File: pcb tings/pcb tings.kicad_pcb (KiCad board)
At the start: 2 copper layers, 24 parts, among them SW1 SW_Push, U1 ATmega32U4-A, Y1 16MHz

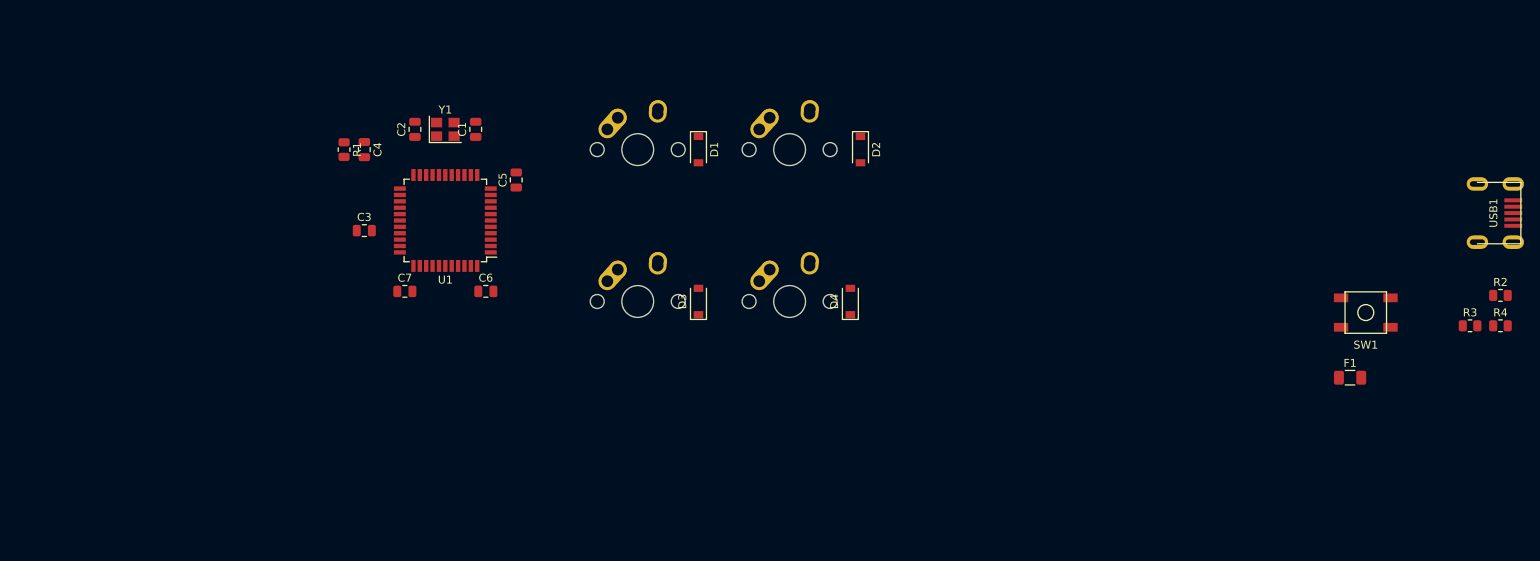
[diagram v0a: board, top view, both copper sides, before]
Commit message: creating pcb edge cuts
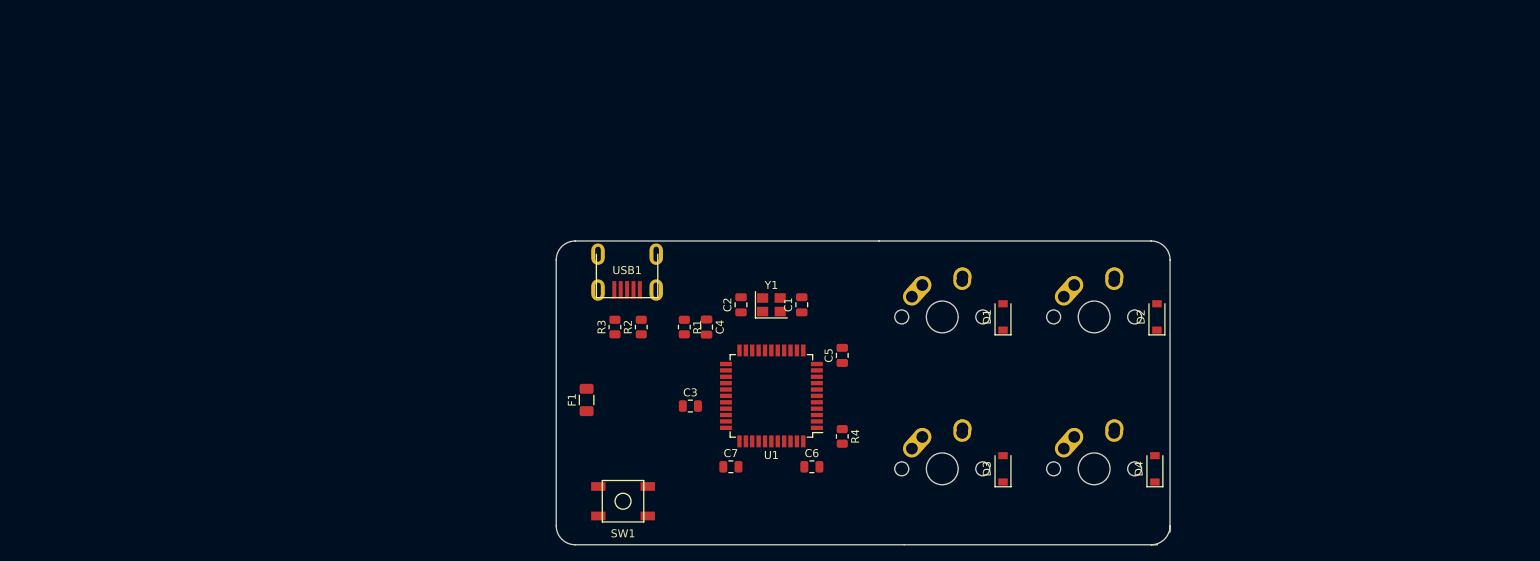
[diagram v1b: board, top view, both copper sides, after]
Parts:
- moved R2 107.8 mm to (123.4, 100.5), turned to 90 degrees
- moved R3 107.3 mm to (120.1, 100.5), turned to 90 degrees
- moved USB1 106.8 mm to (121.6, 91.3), turned to -90 degrees
- moved SW1 96.1 mm to (121.1, 122.3)
- moved F1 95.8 mm to (116.5, 109.6), turned to 90 degrees
- moved R4 83.7 mm to (148.6, 114.2), turned to -90 degrees
- moved C4 48.4 mm to (131.6, 100.5)
- moved R1 48.1 mm to (128.8, 100.5)
- moved C6 46.4 mm to (144.8, 118.0)
- moved C7 46.4 mm to (134.6, 118.0)
- moved C5 46.4 mm to (148.6, 104.0)
- moved C1 46.4 mm to (143.5, 97.7)
- moved C2 46.4 mm to (135.9, 97.7)
- moved C3 46.4 mm to (129.5, 110.4)
- moved U1 46.4 mm to (139.7, 109.1)
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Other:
- board outline added: 77 x 38.1 mm

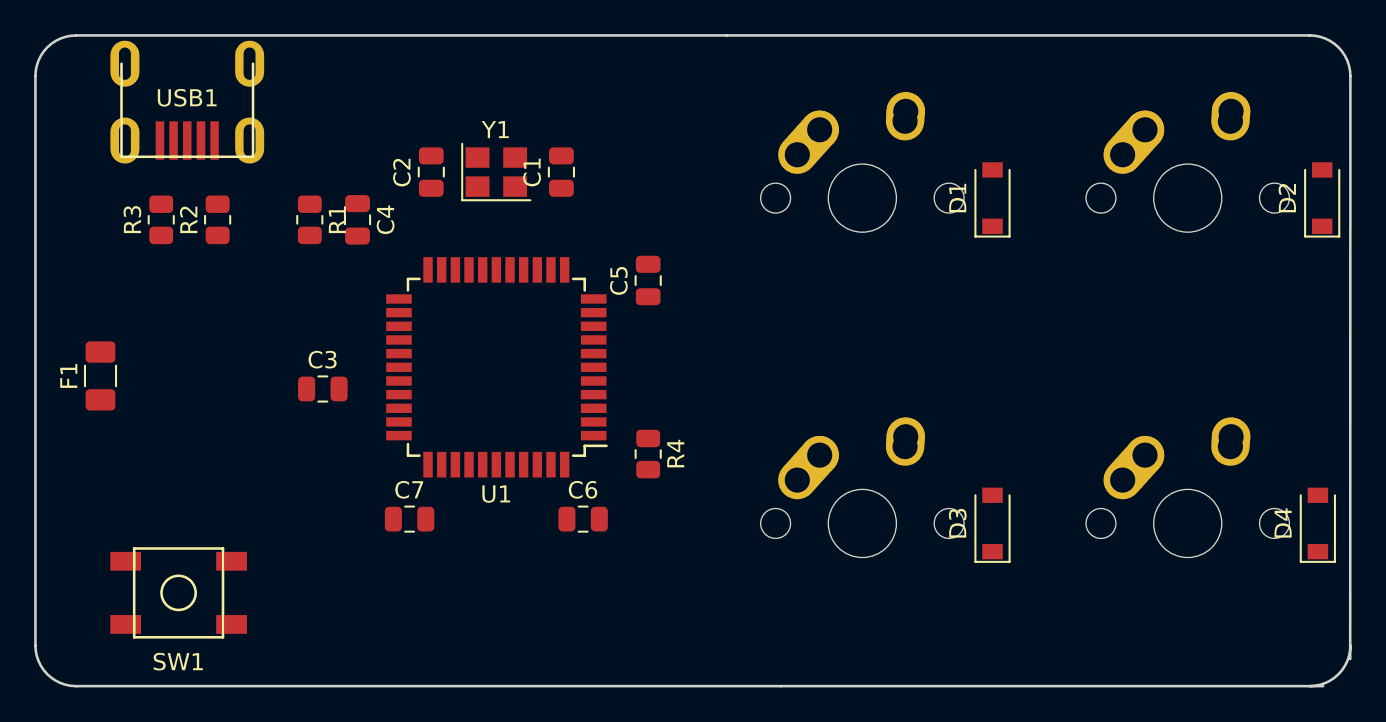
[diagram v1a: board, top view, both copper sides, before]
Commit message: Fixed footprints and edgecuts
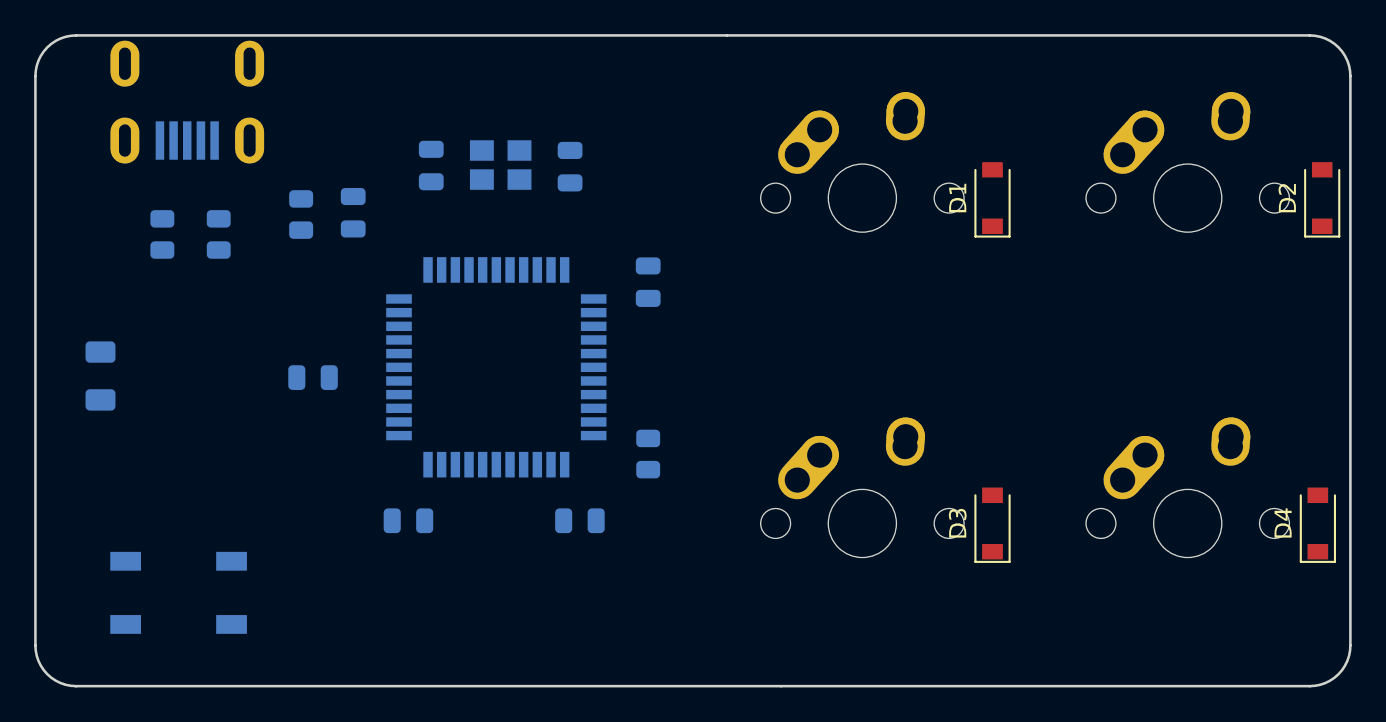
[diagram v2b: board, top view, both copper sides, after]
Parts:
- C1: renamed from C3; moved to B.Cu
- C2: renamed from C4; moved to B.Cu
- C3: renamed from C7; moved to B.Cu
- C4: renamed from C1; moved to B.Cu
- C5: renamed from C2; moved to B.Cu
- C6: renamed from C5; moved to B.Cu
- C7: renamed from C6; moved to B.Cu
- F1, R2, R4, SW1, U1, USB1, Y1: moved to B.Cu
- R1: renamed from R3; moved to B.Cu
- R3: renamed from R1; moved to B.Cu
- moved C1 19.5 mm to (144.0, 97.4), turned to 90 degrees
- moved C6 14.6 mm to (144.6, 118.1), turned to 180 degrees
- moved C5 14.2 mm to (148.6, 104.1)
- moved C4 12.4 mm to (131.3, 100.1)
- moved C7 10.2 mm to (134.6, 118.1)
- moved C3 10.0 mm to (129.0, 109.7), turned to 180 degrees
- moved R3 8.68 mm to (120.1, 101.3), turned to 90 degrees
- moved R1 8.20 mm to (128.3, 100.2)
- moved C2 5.36 mm to (135.9, 97.3)
- moved R2 0.86 mm to (123.4, 101.3)
- moved Y1 0.48 mm to (140.0, 97.3), turned to 180 degrees
- turned F1 to -90 degrees
- turned R4 to 90 degrees
- turned SW1 to 180 degrees
- turned U1 to 0 degrees
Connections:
- U1 pad 27: unconnected-(U1-Pad27) -> ROW0
- U1 pad 28: unconnected-(U1-Pad28) -> COL1
- U1 pad 29: unconnected-(U1-Pad29) -> COL0
- U1 pad 30: unconnected-(U1-Pad30) -> ROW1
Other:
- outline, holes or cut-outs redrawn

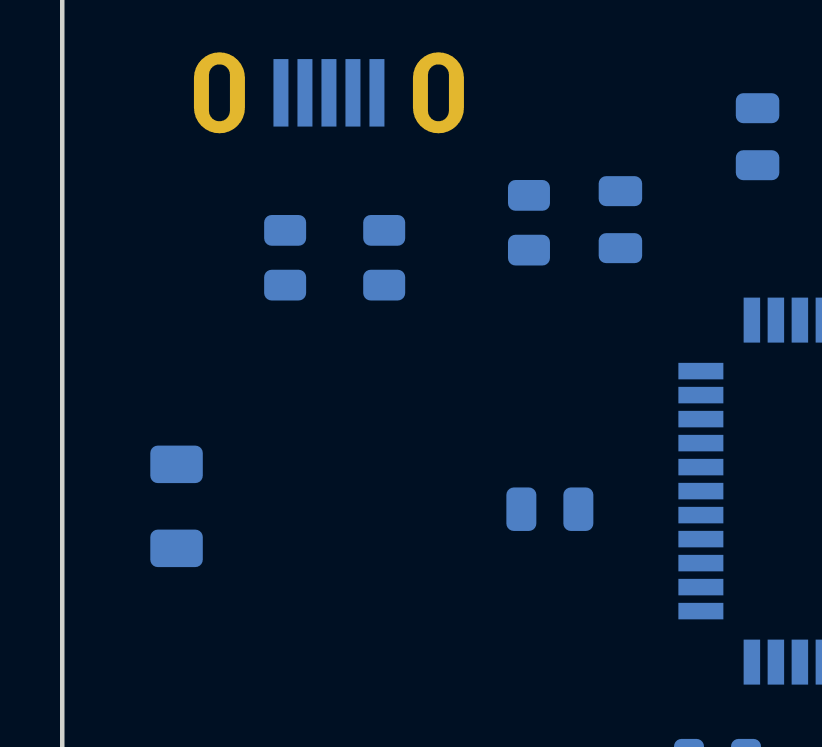
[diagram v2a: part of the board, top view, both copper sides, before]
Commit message: fixed connections (ratsnest)
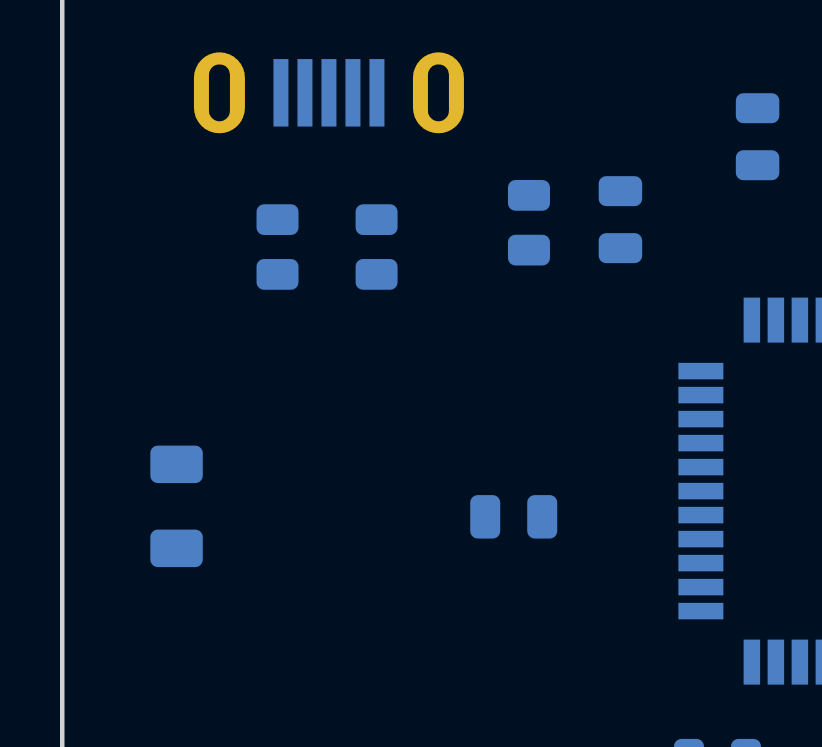
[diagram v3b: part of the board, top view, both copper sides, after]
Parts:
- moved C3 1.23 mm to (127.8, 110.0)
- moved R2 0.44 mm to (123.2, 101.0)
- moved R3 0.44 mm to (119.9, 101.0)
- turned F1 to 90 degrees
- turned R1 to -90 degrees
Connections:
- C1 pad 1: GND -> Net-(U1-Pad17)
- C1 pad 2: Net-(C1-Pad2) -> GND
- C2 pad 1: GND -> Net-(U1-Pad16)
- C2 pad 2: Net-(C2-Pad2) -> GND
- F1 pad 1: VCC -> +5V
- F1 pad 2: +5V -> VCC
- R2 pad 1: unconnected-(R2-Pad1) -> Net-(U1-Pad4)
- R2 pad 2: Net-(R2-Pad2) -> Net-(USB1-Pad3)
- R3 pad 1: unconnected-(R3-Pad1) -> Net-(U1-Pad3)
- R3 pad 2: Net-(R3-Pad2) -> Net-(USB1-Pad4)
- R4 pad 1: Net-(R4-Pad1) -> GND
- R4 pad 2: GND -> Net-(U1-Pad33)
- U1 pad 16: Net-(C2-Pad2) -> Net-(U1-Pad16)
- U1 pad 17: Net-(C1-Pad2) -> Net-(U1-Pad17)
- U1 pad 3: Net-(R3-Pad2) -> Net-(U1-Pad3)
- U1 pad 33: Net-(R4-Pad1) -> Net-(U1-Pad33)
- U1 pad 4: Net-(R2-Pad2) -> Net-(U1-Pad4)
- USB1 pad 3: D+ -> Net-(USB1-Pad3)
- USB1 pad 4: D- -> Net-(USB1-Pad4)
- Y1 pad 1: Net-(C1-Pad2) -> Net-(U1-Pad17)
- Y1 pad 3: Net-(C2-Pad2) -> Net-(U1-Pad16)

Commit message: Routing
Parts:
- D1, D2, D3, D4: moved to B.Cu
- moved C7 78.2 mm to (62.7, 87.1), turned to -90 degrees
- moved F1 74.2 mm to (48.8, 79.2)
- moved R2 73.4 mm to (55.1, 73.7)
- moved R3 73.4 mm to (51.8, 73.7)
- moved D4 73.3 mm to (120.2, 90.0)
- moved USB1 73.3 mm to (53.9, 63.2)
- moved D1 73.3 mm to (101.1, 71.1)
- moved D2 73.3 mm to (120.4, 71.1)
- moved MX1 73.3 mm to (93.4, 71.1)
- moved MX2 73.3 mm to (112.5, 71.1)
- moved MX4 73.3 mm to (112.5, 90.1)
- moved SW1 73.3 mm to (53.4, 94.2)
- moved D3 73.3 mm to (101.1, 90.2)
- moved MX3 73.3 mm to (93.5, 90.2)
- moved C2 73.0 mm to (68.5, 69.2)
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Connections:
- net Net-(USB1-Pad3) renamed D+
- net Net-(USB1-Pad4) renamed D-
- C1 pad 2: GND -> +5V
- C2 pad 2: GND -> +5V
- C3 pad 2: GND -> +5V
- C4 pad 2: GND -> +5V
- C5 pad 2: GND -> +5V
- C6 pad 2: GND -> +5V
- C7 pad 2: GND -> +5V
- D1 pad 1: Net-(D1-Pad1) -> ROW0
- D2 pad 1: Net-(D1-Pad1) -> ROW0
- D3 pad 1: Net-(D3-Pad1) -> ROW1
- D4 pad 1: Net-(D3-Pad1) -> ROW1
- R4 pad 1: GND -> +5V
- SW1 pad 1: GND -> +5V
- U1 pad 15: GND -> +5V
- U1 pad 23: GND -> +5V
- U1 pad 35: GND -> +5V
- U1 pad 43: GND -> +5V
- U1 pad 5: GND -> +5V
- USB1 pad 1: GND -> +5V
- Y1 pad 2: GND -> +5V
- Y1 pad 4: GND -> +5V
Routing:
- net +5V: track 0.00 -> 241.4 mm, vias 0 -> 5
- net COL1: track 0.00 -> 51.7 mm
- net ROW1: track 0.00 -> 49.9 mm
- net ROW0: track 0.00 -> 46.6 mm
- net COL0: track 0.00 -> 32.4 mm
- net Net-(R1-Pad2): track 0.00 -> 32.0 mm, vias 0 -> 2
- net Net-(U1-Pad3): track 0.00 -> 21.4 mm
- net Net-(U1-Pad4): track 0.00 -> 20.6 mm
- net Net-(U1-Pad16): track 0.00 -> 12.7 mm
- net VCC: track 0.00 -> 11.6 mm
- net Net-(U1-Pad17): track 0.00 -> 9.76 mm
- net Net-(D2-Pad2): track 0.00 -> 6.58 mm
- net Net-(D3-Pad2): track 0.00 -> 6.30 mm
- net Net-(D1-Pad2): track 0.00 -> 6.30 mm
- net Net-(D4-Pad2): track 0.00 -> 6.30 mm
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
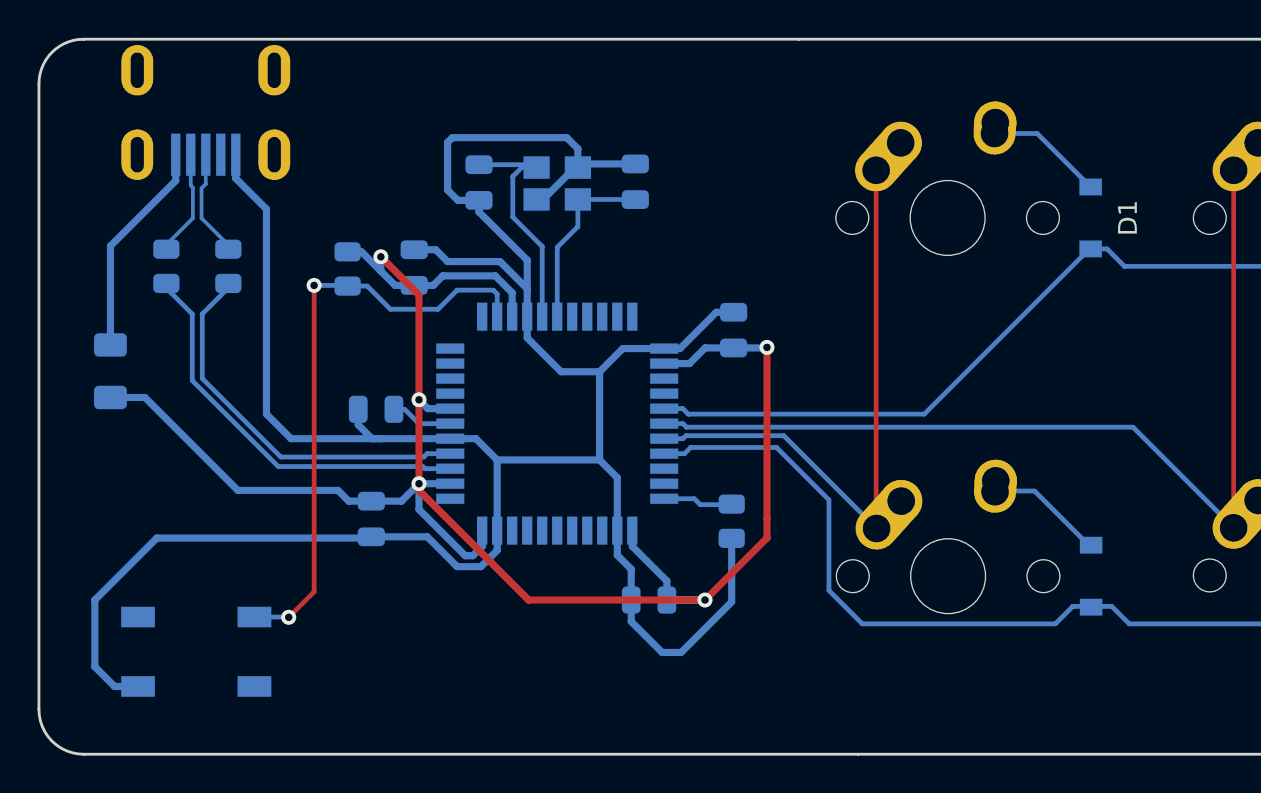
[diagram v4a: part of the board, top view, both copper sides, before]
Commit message: fill zones (check for "unconnected" error)
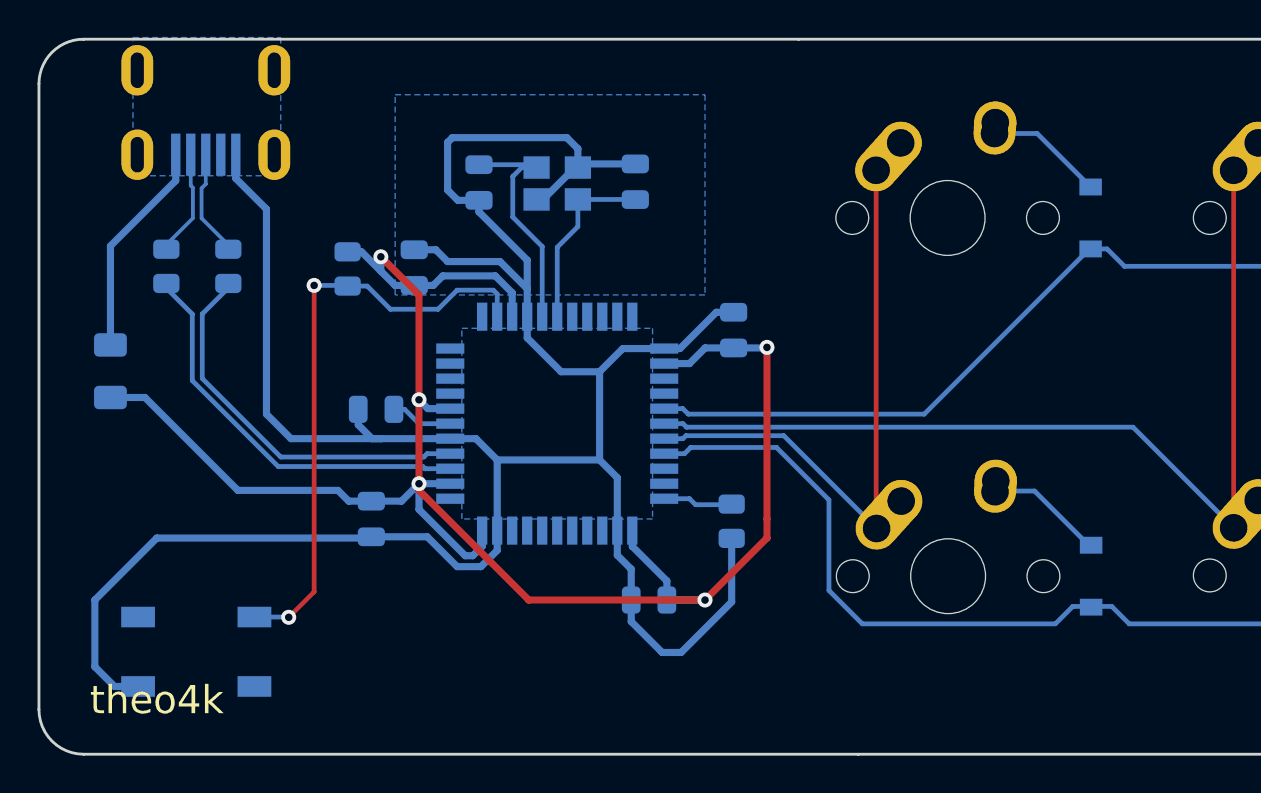
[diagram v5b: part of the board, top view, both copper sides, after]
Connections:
- C1 pad 2: +5V -> GND
- C2 pad 2: +5V -> GND
- C3 pad 2: +5V -> GND
- C4 pad 2: +5V -> GND
- C5 pad 2: +5V -> GND
- C6 pad 2: +5V -> GND
- C7 pad 2: +5V -> GND
- R4 pad 1: +5V -> GND
- SW1 pad 1: +5V -> GND
- U1 pad 15: +5V -> GND
- U1 pad 23: +5V -> GND
- U1 pad 35: +5V -> GND
- U1 pad 43: +5V -> GND
- U1 pad 5: +5V -> GND
- USB1 pad 1: +5V -> GND
- Y1 pad 2: +5V -> GND
- Y1 pad 4: +5V -> GND
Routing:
- net +5V: track 241.4 -> 99.7 mm
- net GND: track 0.00 -> 141.8 mm
- added copper zone on B.Cu, net GND
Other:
- rule pad_to_mask_clearance: 0 -> 0.2
- board text added: "theo4k"
